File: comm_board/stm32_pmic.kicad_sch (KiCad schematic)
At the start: 14 parts, among them U13 STM32L496RGTx

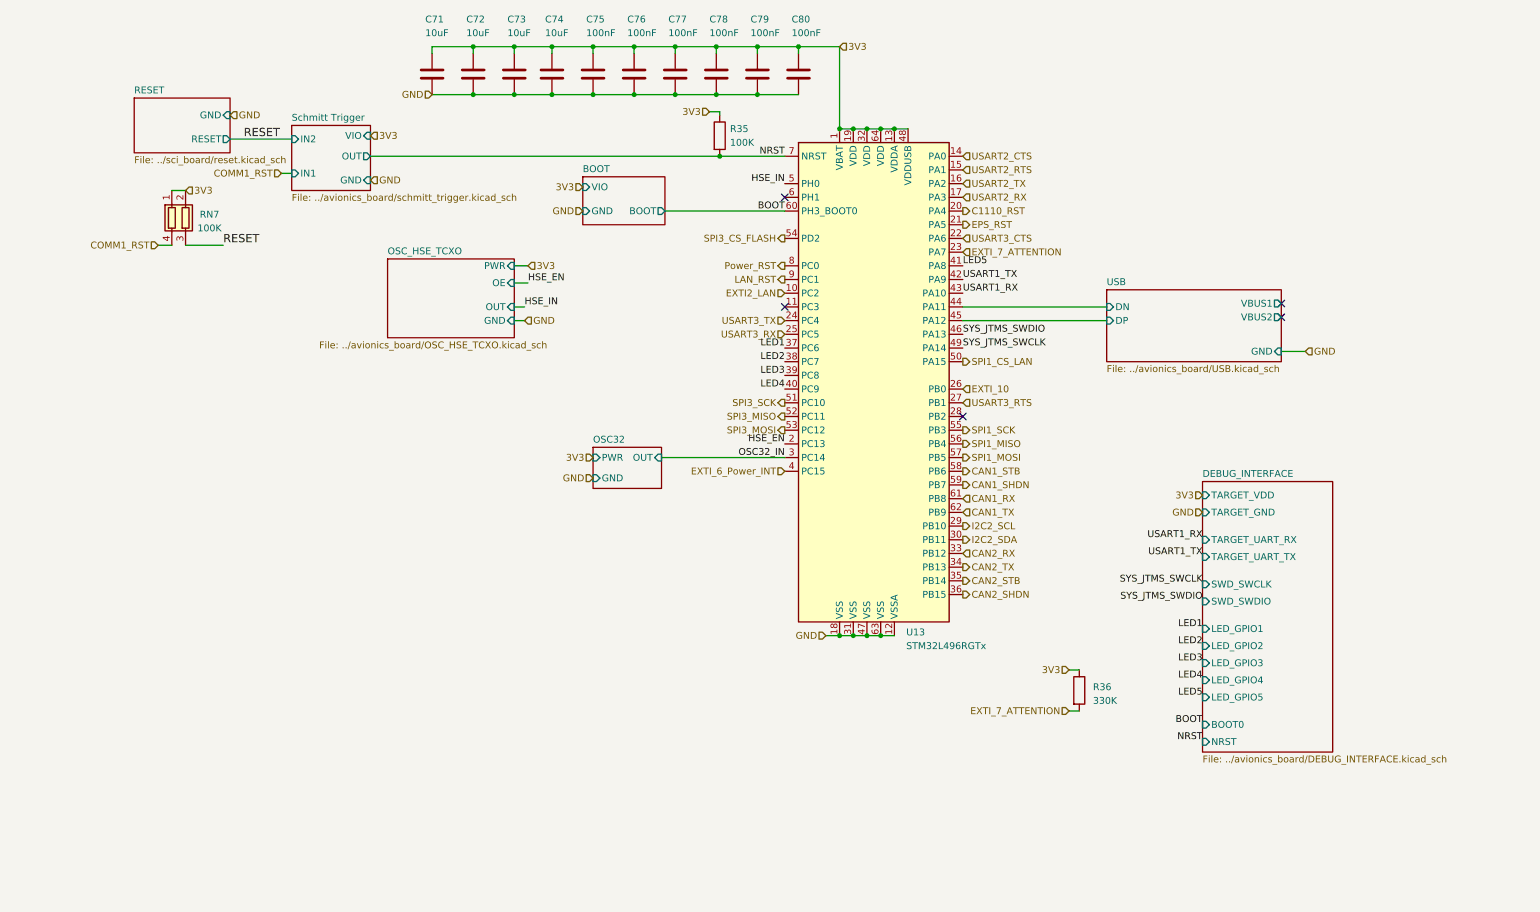
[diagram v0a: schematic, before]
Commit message: Comm board update with CC1101 and CC1090 on 915MHz
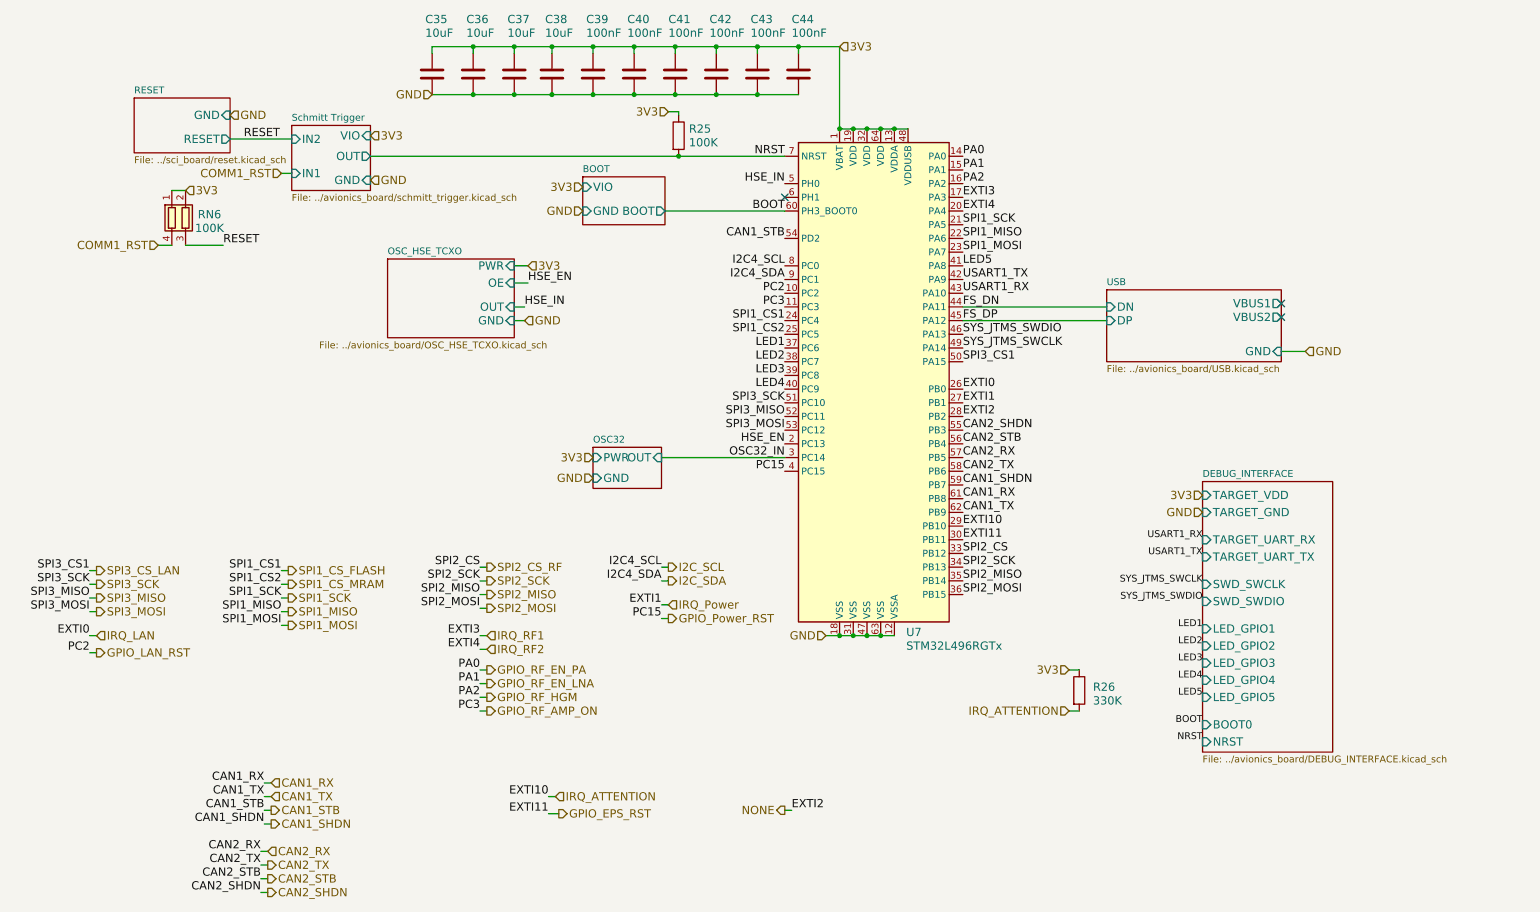
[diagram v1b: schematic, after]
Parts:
- renumbered C71 to C35, C72 to C36, C73 to C37, C74 to C38, C75 to C39, C76 to C40, C77 to C41, C78 to C42, C79 to C43, C80 to C44, R35 to R25, R36 to R26, RN7 to RN6, U13 to U7
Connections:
- net EPS_RST is gone; now on net SPI1_SCK: U7.21 (PA5)
- net I2C2_SCL is gone; now on net IRQ_ATTENTION: U7.29 (PB10)
- net SPI3_CS_FLASH is gone; now on net CAN1_STB: U7.54 (PD2)
- net USART3_CTS is gone; now on net SPI1_MISO: U7.22 (PA6)
- net CAN1_STB: no longer U7.58 (PB6)
- net CAN2_RX: now also U7.57 (PB5); no longer U7.33 (PB12)
- net CAN2_SHDN: now also U7.55 (PB3); no longer U7.36 (PB15)
- net CAN2_STB: now also U7.56 (PB4); no longer U7.35 (PB14)
- net CAN2_TX: now also U7.58 (PB6); no longer U7.34 (PB13)
- net SPI1_MISO: no longer U7.56 (PB4)
- net SPI1_MOSI: now also U7.23 (PA7); no longer U7.57 (PB5)
- net SPI1_SCK: no longer U7.55 (PB3)
- net GPIO_RF_AMP_ON: now reaches U7.11 (PC3)
- net NONE: now reaches U7.28 (PB2)
- net C1110_RST renamed IRQ_RF2
- net EXTI2_LAN renamed GPIO_LAN_RST
- net EXTI_10 renamed IRQ_LAN
- net EXTI_6_Power_INT renamed GPIO_Power_RST
- net EXTI_7_ATTENTION renamed IRQ_ATTENTION
- net IRQ_ATTENTION: no longer U7.23 (PA7)
- net I2C2_SDA renamed GPIO_EPS_RST
- net LAN_RST renamed I2C_SDA
- net Power_RST renamed I2C_SCL
- net SPI1_CS_LAN renamed SPI3_CS_LAN
- net USART2_CTS renamed GPIO_RF_EN_PA
- net USART2_RTS renamed GPIO_RF_EN_LNA
- net USART2_RX renamed IRQ_RF1
- net USART2_TX renamed GPIO_RF_HGM
- net USART3_RTS renamed IRQ_Power
- net USART3_RX renamed SPI1_CS_MRAM
- net USART3_TX renamed SPI1_CS_FLASH
- net USB/DN renamed FS_DN
- net USB/DP renamed FS_DP
- new net SPI2_CS_RF: U7.33 (PB12)
- new net SPI2_MISO: U7.35 (PB14)
- new net SPI2_MOSI: U7.36 (PB15)
- new net SPI2_SCK: U7.34 (PB13)
- no-connect marks 5 -> 3
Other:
- moved on the sheet: R25

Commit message: move commonly used hierarchical sheets to common/sheets for easy reuse
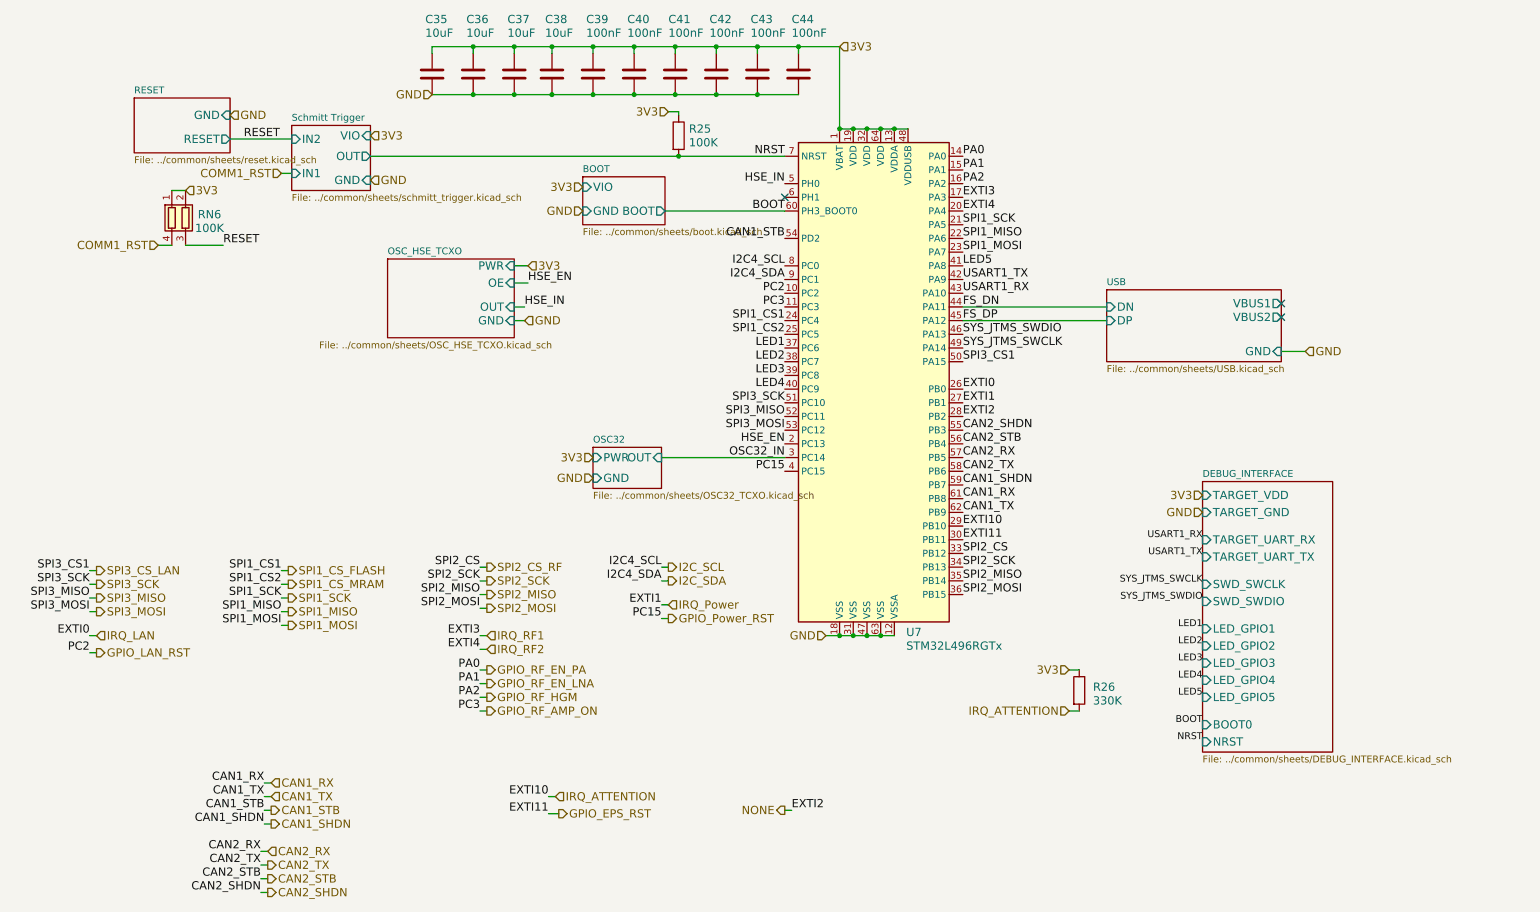
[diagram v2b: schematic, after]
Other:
- sheet BOOT: file ../avionics_board/boot.kicad_sch -> ../common/sheets/boot.kicad_sch
- sheet DEBUG_INTERFACE: file ../avionics_board/DEBUG_INTERFACE.kicad_sch -> ../common/sheets/DEBUG_INTERFACE.kicad_sch
- sheet OSC32: file ../avionics_board/OSC32_TCXO.kicad_sch -> ../common/sheets/OSC32_TCXO.kicad_sch
- sheet OSC_HSE_TCXO: file ../avionics_board/OSC_HSE_TCXO.kicad_sch -> ../common/sheets/OSC_HSE_TCXO.kicad_sch
- sheet RESET: file ../sci_board/reset.kicad_sch -> ../common/sheets/reset.kicad_sch
- sheet Schmitt Trigger: file ../avionics_board/schmitt_trigger.kicad_sch -> ../common/sheets/schmitt_trigger.kicad_sch
- sheet USB: file ../avionics_board/USB.kicad_sch -> ../common/sheets/USB.kicad_sch
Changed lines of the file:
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@@
 			)
 		)
-		(property "Sheetfile" "../avionics_board/boot.kicad_sch"
+		(property "Sheetfile" "../common/sheets/boot.kicad_sch"
 			(at 118.745 65.9896 0)
 			(effects
@@
 				)
 				(justify left top)
-				(hide yes)
 			)
 		)
@@
 		)
 		(instances
-			(project "openlst-hw"
+			(project "comm_board"
 				(path "/a863a5ec-a5d4-4f54-be53-e8c01d5e3ac4/53f12969-e593-459a-9671-cc23a5a9aea0/f4ff56ce-2fa2-4b99-a709-c113709260c1"
 					(page "13")
@@
 			)
 		)
-		(property "Sheetfile" "../avionics_board/OSC_HSE_TCXO.kicad_sch"
+		(property "Sheetfile" "../common/sheets/OSC_HSE_TCXO.kicad_sch"
 			(at 69.85 86.995 0)
 			(effects
@@
 		)
 		(instances
-			(project "openlst-hw"
+			(project "comm_board"
 				(path "/a863a5ec-a5d4-4f54-be53-e8c01d5e3ac4/53f12969-e593-459a-9671-cc23a5a9aea0/f4ff56ce-2fa2-4b99-a709-c113709260c1"
 					(page "4")
@@
 			)
 		)
-		(property "Sheetfile" "../avionics_board/schmitt_trigger.kicad_sch"
+		(property "Sheetfile" "../common/sheets/schmitt_trigger.kicad_sch"
 			(at 64.77 59.6396 0)
 			(effects
@@
 		)
 		(instances
-			(project "openlst-hw"
+			(project "comm_board"
 				(path "/a863a5ec-a5d4-4f54-be53-e8c01d5e3ac4/53f12969-e593-459a-9671-cc23a5a9aea0/f4ff56ce-2fa2-4b99-a709-c113709260c1"
 					(page "13")
@@
 			)
 		)
-		(property "Sheetfile" "../avionics_board/OSC32_TCXO.kicad_sch"
+		(property "Sheetfile" "../common/sheets/OSC32_TCXO.kicad_sch"
 			(at 120.65 114.8846 0)
 			(effects
@@
 				)
 				(justify left top)
-				(hide yes)
 			)
 		)
@@
 		)
 		(instances
-			(project "openlst-hw"
+			(project "comm_board"
 				(path "/a863a5ec-a5d4-4f54-be53-e8c01d5e3ac4/53f12969-e593-459a-9671-cc23a5a9aea0/f4ff56ce-2fa2-4b99-a709-c113709260c1"
 					(page "16")
@@
 			)
 		)
-		(property "Sheetfile" "../sci_board/reset.kicad_sch"
+		(property "Sheetfile" "../common/sheets/reset.kicad_sch"
 			(at 35.56 52.6546 0)
 			(effects
@@
 		)
 		(instances
-			(project "openlst-hw"
+			(project "comm_board"
 				(path "/a863a5ec-a5d4-4f54-be53-e8c01d5e3ac4/53f12969-e593-459a-9671-cc23a5a9aea0/f4ff56ce-2fa2-4b99-a709-c113709260c1"
 					(page "14")
@@
 			)
 		)
-		(property "Sheetfile" "../avionics_board/USB.kicad_sch"
+		(property "Sheetfile" "../common/sheets/USB.kicad_sch"
 			(at 215.9 91.3896 0)
 			(effects
@@
 		)
 		(instances
-			(project "openlst-hw"
+			(project "comm_board"
 				(path "/a863a5ec-a5d4-4f54-be53-e8c01d5e3ac4/53f12969-e593-459a-9671-cc23a5a9aea0/f4ff56ce-2fa2-4b99-a709-c113709260c1"
 					(page "13")
@@
 			)
 		)
-		(property "Sheetfile" "../avionics_board/DEBUG_INTERFACE.kicad_sch"
+		(property "Sheetfile" "../common/sheets/DEBUG_INTERFACE.kicad_sch"
 			(at 233.68 163.7796 0)
 			(effects
@@
 		)
 		(instances
-			(project "openlst-hw"
+			(project "comm_board"
 				(path "/a863a5ec-a5d4-4f54-be53-e8c01d5e3ac4/53f12969-e593-459a-9671-cc23a5a9aea0/f4ff56ce-2fa2-4b99-a709-c113709260c1"
 					(page "13")

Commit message: moving common sheets to common, cleanup for some missed files
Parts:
- C35, C36, C37, C38: value 10uF -> 10u
- C39, C40, C41, C42, C43, C44: value 100nF -> 100n
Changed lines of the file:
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@@
 			)
 		)
-		(property "Value" "100nF"
+		(property "Value" "100n"
 			(at 157.48 29.845 0)
 			(effects
@@
 			)
 		)
-		(property "Value" "100nF"
+		(property "Value" "100n"
 			(at 149.86 29.845 0)
 			(effects
@@
 			)
 		)
-		(property "Value" "100nF"
+		(property "Value" "100n"
 			(at 134.62 29.845 0)
 			(effects
@@
 			)
 		)
-		(property "Value" "10uF"
+		(property "Value" "10u"
 			(at 111.76 29.845 0)
 			(effects
@@
 			)
 		)
-		(property "Value" "100nF"
+		(property "Value" "100n"
 			(at 119.38 29.845 0)
 			(effects
@@
 			)
 		)
-		(property "Value" "10uF"
+		(property "Value" "10u"
 			(at 89.535 29.845 0)
 			(effects
@@
 			)
 		)
-		(property "Value" "100nF"
+		(property "Value" "100n"
 			(at 127 29.845 0)
 			(effects
@@
 			)
 		)
-		(property "Value" "100nF"
+		(property "Value" "100n"
 			(at 142.24 29.845 0)
 			(effects
@@
 			)
 		)
-		(property "Value" "10uF"
+		(property "Value" "10u"
 			(at 97.155 29.845 0)
 			(effects
@@
 			)
 		)
-		(property "Value" "10uF"
+		(property "Value" "10u"
 			(at 104.775 29.845 0)
 			(effects
